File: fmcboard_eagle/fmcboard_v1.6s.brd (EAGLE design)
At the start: 147 x 74 mm, 281 parts, among them IC1 OPA699ID, IC10 LM358, IC11 7805DT, IC12 SN74AUC2G66DCTR, IC13 SN74AUC2G66DCTR, IC14 SN74AUC2G66DCTR, IC15 SN74AUC2G66DCTR, IC16 DAC7578SPWR, IC17 SN74AUC2G66DCTR, IC18 SN74AUC2G66DCTR, IC19 SN74AUC2G66DCTR, IC2 DAC7578SPWR, IC20 SN74AUC2G66DCTR, IC21 74AUP2GU04GW, IC22 74AUP2GU04GW, IC23 74AUP2GU04GW, IC24 74AUP2GU04GW, IC25 MC7905ACD2TR4G, IC26 AMS1117-1.8, IC27 LM358, IC28 SN74AUC2G66DCTR, IC29 LM337KVURG3, IC3 LTC6229IMS8E#TRPBF, IC30 SN74AUC2G66DCTR, IC31 SN74AUC2G66DCTR, IC32 SN74AUC2G66DCTR, IC33 LTC6229IMS8E#TRPBF, IC34 74AUP2GU04GW, IC35 74AUP2GU04GW, IC4 OPA695IDR, IC5 LTC6229IMS8E#TRPBF, IC6 OPA695IDR, IC7 OPA699ID, IC8 LM358, IC9 LM358, J1 8pin, J12 4p-2.54, J13 4p-2.54, J2 ASP-134604-01, J3 4p-2.54, J4 4p-2.54, J5 4p-2.54, J6 4p-2.54, J7 4p-2.54, J8 4p-2.54

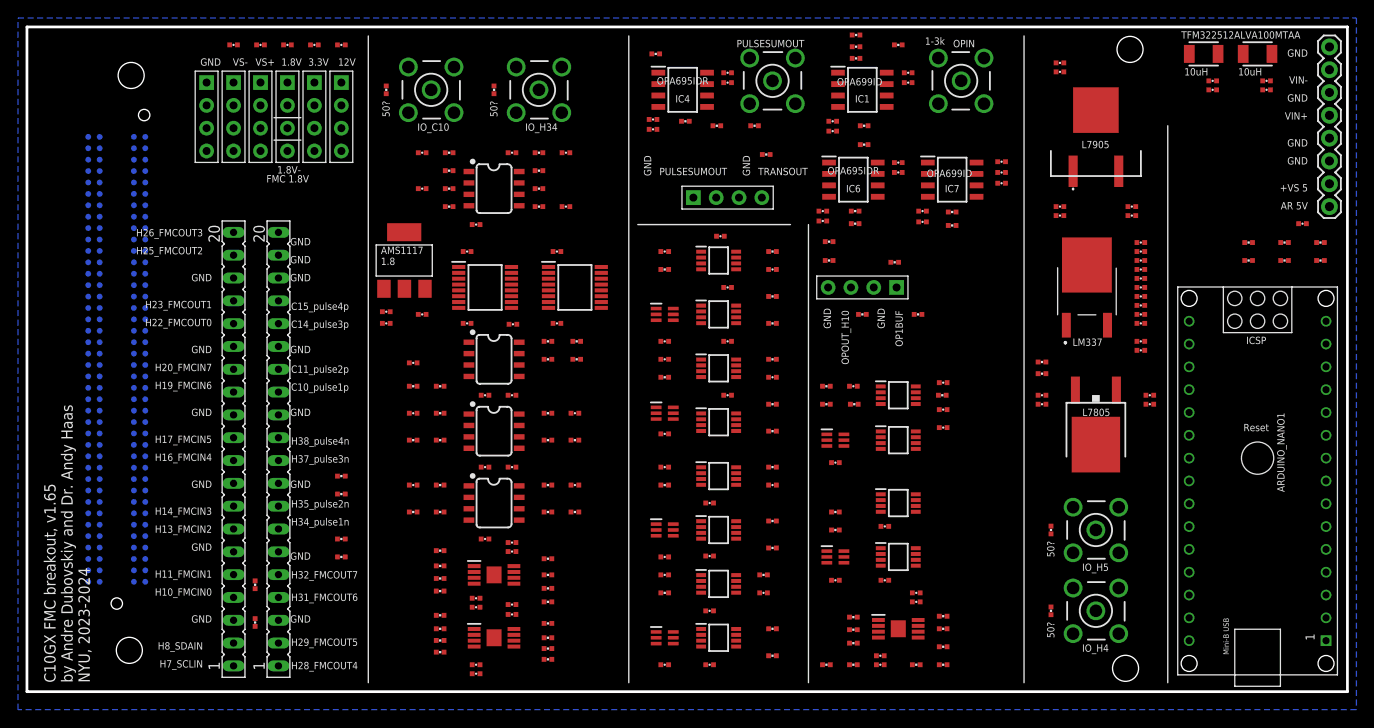
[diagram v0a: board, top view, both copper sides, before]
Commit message: and power +-7 onboard laid out
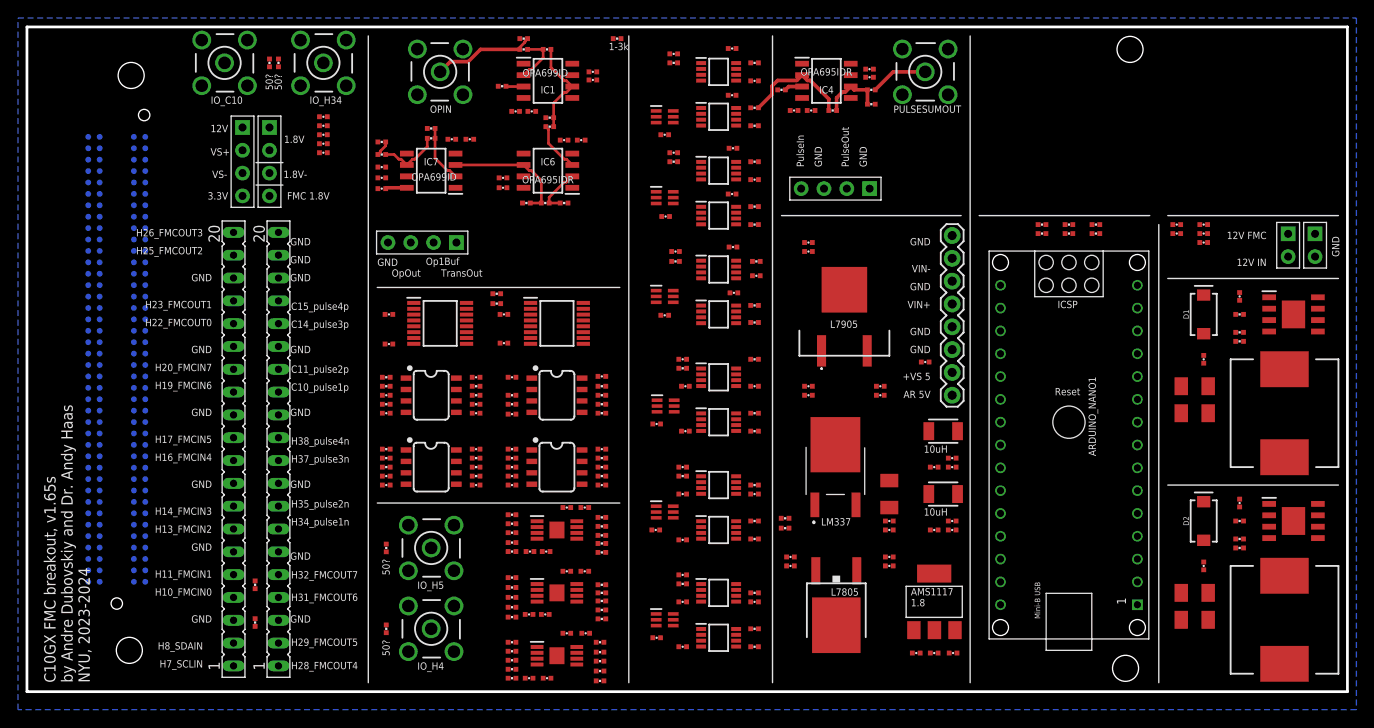
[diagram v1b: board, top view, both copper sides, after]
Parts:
- removed C110, C111, C112, C113, C114, C115: 10uF, passives:0402_CAP
- removed J4, J6, J7: 4p-2.54, Seeed-Connector:H4-2.54
- added C11, C121, C8: 0.1uF, passives:0402_CAP
- added C118, C119, C120, C64, C80: 10uF, passives:0402_CAP
- added C122: 0.01uF, passives:0402_CAP
- added C123, C124, C125: 100uF, rcl:C1206K
- added D1, D2: B340A, SparkFun-DiscreteSemi:SMA-DIODE
- added IC36, IC37: TPS5430DDAR, TPS5430DDAR:SOIC127P600X170-9N
- added J9: 2p-2.54, Seeed-Connector:H2-2.54
- added L3, L4: 10uH, SparkFun-Passives:CDRH125
- added R116, R117, R60, R84: 1k, passives:0402_RES
- added R118, R73: 10k, passives:0402_RES
- C106: value 10uF -> 0.1uF
- C107: value 10uF -> 0.01uF
- C108, C109: value 10uF -> 100uF; device passives:0402_CAP -> rcl:C1206K
- J3: value 4p-2.54 -> 2p-2.54; device Seeed-Connector:H4-2.54 -> Seeed-Connector:H2-2.54
- moved J3 112.3 mm to (143.4, 49.7)
- moved IO_H4 74.0 mm to (45.0, 7.00)
- moved IO_H5 74.0 mm to (45.0, 16.0)
- moved R15 74.0 mm to (40.0, 7.00)
- moved R16 74.0 mm to (40.0, 16.0)
- moved C74 71.2 mm to (101.0, 4.30), turned to 0 degrees
- moved C34 70.2 mm to (99.0, 4.30)
- moved IC26 70.2 mm to (101.0, 10.0)
- moved C3 70.1 mm to (103.1, 4.30), turned to 180 degrees
- moved C7 69.1 mm to (39.5, 56.0), turned to 180 degrees
- moved C28 69.0 mm to (39.5, 58.4), turned to 180 degrees
- moved C87 69.0 mm to (39.5, 57.2), turned to 180 degrees
- moved R88 62.3 mm to (39.5, 59.8)
- moved C41 60.2 mm to (103.0, 18.0)
- moved C44 60.2 mm to (103.0, 19.0)
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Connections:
- new net ARVIN: ARDUINO_NANO1.15
- new net BOOT1: C122.1, IC37.1
- new net BOOT2: C107.1, IC36.1
- new net FB1: IC37.4, R60.2, R73.1
- new net FB2: IC36.4, R116.2, R118.1
- new net N$29: C120.1, C64.2
- new net N$36: J5.2, R72.1
- new net N$39: C119.2, C41.1
- new net N$52: C120.2, C80.1
- new net N$53: C123.1, C124.2
- new net N$54: R60.1, R84.2
- new net N$55: C108.1, C109.2
- new net N$56: R116.1, R117.2
- new net SW1: C122.2, D1.C, IC37.8, L3.1
- new net SW2: C107.2, D2.C, IC36.8, L4.1
- new net V-: IC36.6, IC36.9
- net 12V: now also J9.1; no longer J8.2, J8.3, J8.4
- net 1V8-: now also C125.1; no longer C106.1, C107.1, C108.1, C109.1, C110.1, C111.1, C112.1, C113.1, C114.1, C115.1
- net 3V3: now also J8.4; no longer J3.1, J3.2, J3.3, J3.4
- net GND: now also C106.1, C109.1, C11.2, C119.1, C121.2, C123.2, C125.2, C8.2, C80.2, D1.A, IC37.6, IC37.9, J3.1, J3.2, L4.2, R118.2, R84.1; no longer C106.2, C107.2, C108.2, C109.2, C110.2, C111.2, C112.2, C113.2, C114.2, C115.2, C41.1, J4.1, J4.2, J4.3, J4.4, J5.2
- net N$38: now also C1.1, C118.2; no longer J13.4, R72.1
- net OP1BUF: now also R72.2; no longer R89.2
- net PULSESUMIN: now also J13.4
- net TRANSOUT: now also R89.2; no longer R72.2
- net VIN: now also C11.1, C64.1, C8.1, IC36.7, IC37.7, J9.2; no longer ARDUINO_NANO1.15
- net VIN+: now also C118.1, C121.1, C124.1, L3.2, R73.2; no longer C1.1
- net VIN-: now also C106.2, C108.2, D2.A, R117.1
- net VS+: now also J8.2; no longer J6.1, J6.2, J6.3, J6.4
- net VS-: now also J8.3; no longer J7.1, J7.2, J7.3, J7.4
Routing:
- net OP1BUF: track 0.00 -> 14.0 mm
- net PULSESUMIN: track 0.00 -> 12.3 mm
- net IO1: track 0.00 -> 11.5 mm
- net TRANSOUT: track 0.00 -> 10.7 mm
- net PULSESUMOUT: track 0.00 -> 7.11 mm
- net OP2OUT: track 0.00 -> 6.89 mm
- net N$11: track 0.00 -> 6.43 mm
- net PULSEOUT: track 0.00 -> 6.40 mm
- net TRANSIN: track 0.00 -> 5.65 mm
- net N$10: track 0.00 -> 5.63 mm
- net N$9: track 0.00 -> 5.41 mm
- net 1V8: track 0.00 -> 2.40 mm
- net N$8: track 0.00 -> 2.01 mm
- net N$3: track 0.00 -> 1.97 mm
- net OPOUT_H10: track 0.00 -> 1.76 mm
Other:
- board text added: "12V FMC"
- board text added: "12V IN"
- board text added: "C10GX FMC breakout, v1.65s by Andre Dubovskiy and Dr. Andy Haas NYU, 2023-2024"
- board text added: "Op1Buf"
- board text added: "OpOut"
- board text added: "PulseIn"
- board text added: "PulseOut"
- board text added: "TransOut"
- board text removed: "C10GX FMC breakout, v1.65 by Andre Dubovskiy and Dr. Andy Haas NYU, 2023-2024"
- board text removed: "OP1BUF"
- board text removed: "OPOUT_H10"
- board text removed: "PULSESUMOUT"
- board text removed: "TRANSOUT"

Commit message: power routed
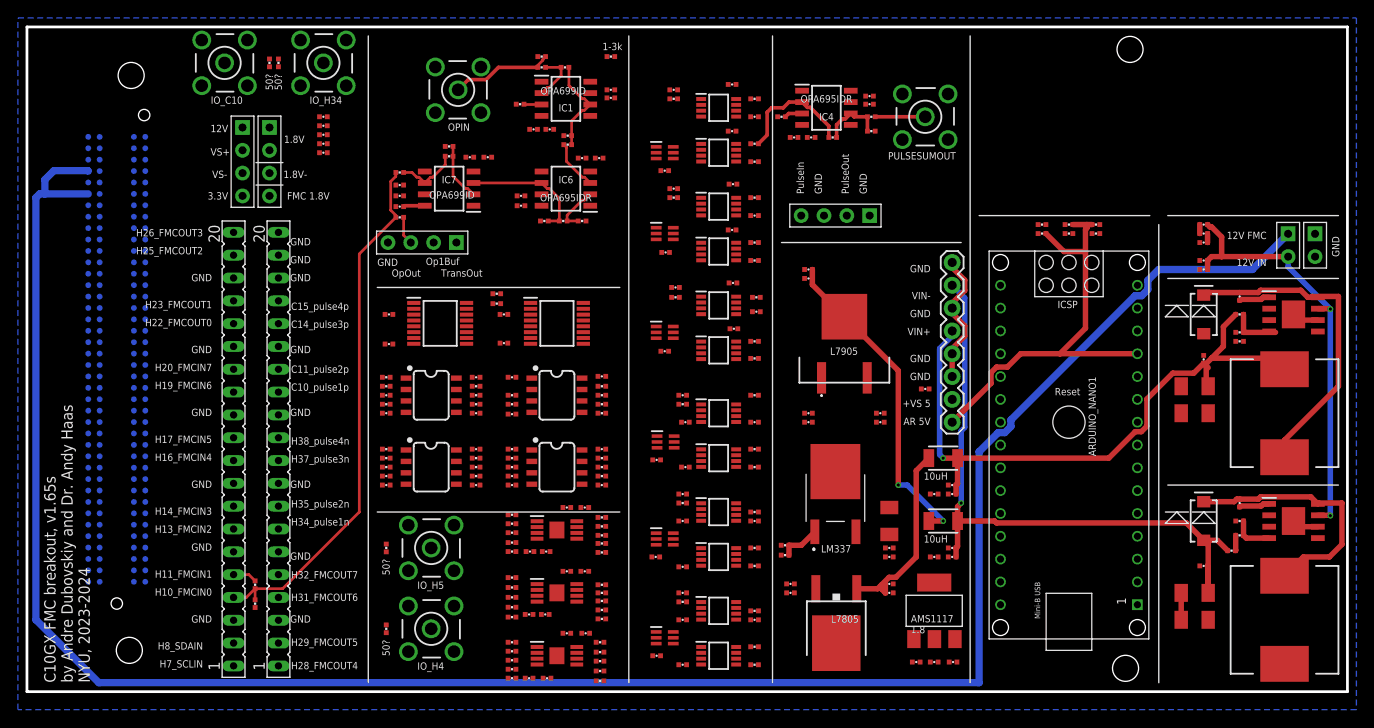
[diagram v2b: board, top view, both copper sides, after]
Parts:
- moved R86 8.63 mm to (41.5, 52.8), turned to 180 degrees
- moved C11 5.00 mm to (131.0, 48.0), turned to 180 degrees
- moved C8 5.00 mm to (131.0, 47.0), turned to 180 degrees
- moved PULSESUMOUT 5.00 mm to (100.0, 64.0)
- moved C52 4.00 mm to (78.5, 62.4)
- moved C100 4.00 mm to (81.0, 30.0)
- moved C101 4.00 mm to (73.3, 30.0)
- moved C102 4.00 mm to (78.6, 45.5)
- moved C103 4.00 mm to (78.7, 40.4)
- moved C104 4.00 mm to (73.3, 25.0)
- moved C105 4.00 mm to (71.0, 37.9)
- moved C30 4.00 mm to (70.1, 25.8)
- moved C31 4.00 mm to (81.2, 42.3)
- moved C35 4.00 mm to (78.5, 67.6)
- moved C49 4.00 mm to (71.1, 48.9)
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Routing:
- net 12V: track 0.00 -> 238.9 mm
- net VIN+: track 0.00 -> 73.4 mm, vias 0 -> 1
- net VIN-: track 0.00 -> 71.7 mm, vias 0 -> 1
- net OPOUT_H10: track 1.76 -> 59.1 mm
- net VIN: track 0.00 -> 48.1 mm, vias 0 -> 2
- net AR_5V: track 0.00 -> 47.5 mm
- net SW1: track 0.00 -> 36.7 mm
- net VIN-CLEAN: track 0.00 -> 36.2 mm, vias 0 -> 2
- net SW2: track 0.00 -> 28.4 mm
- net VIN+CLEAN: track 0.00 -> 21.7 mm
- net GND: track 0.00 -> 18.0 mm
- net FB1: track 0.00 -> 5.57 mm
- net N$30: track 0.00 -> 4.60 mm
- net FB2: track 0.00 -> 4.58 mm
- net BOOT2: track 0.00 -> 3.43 mm
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
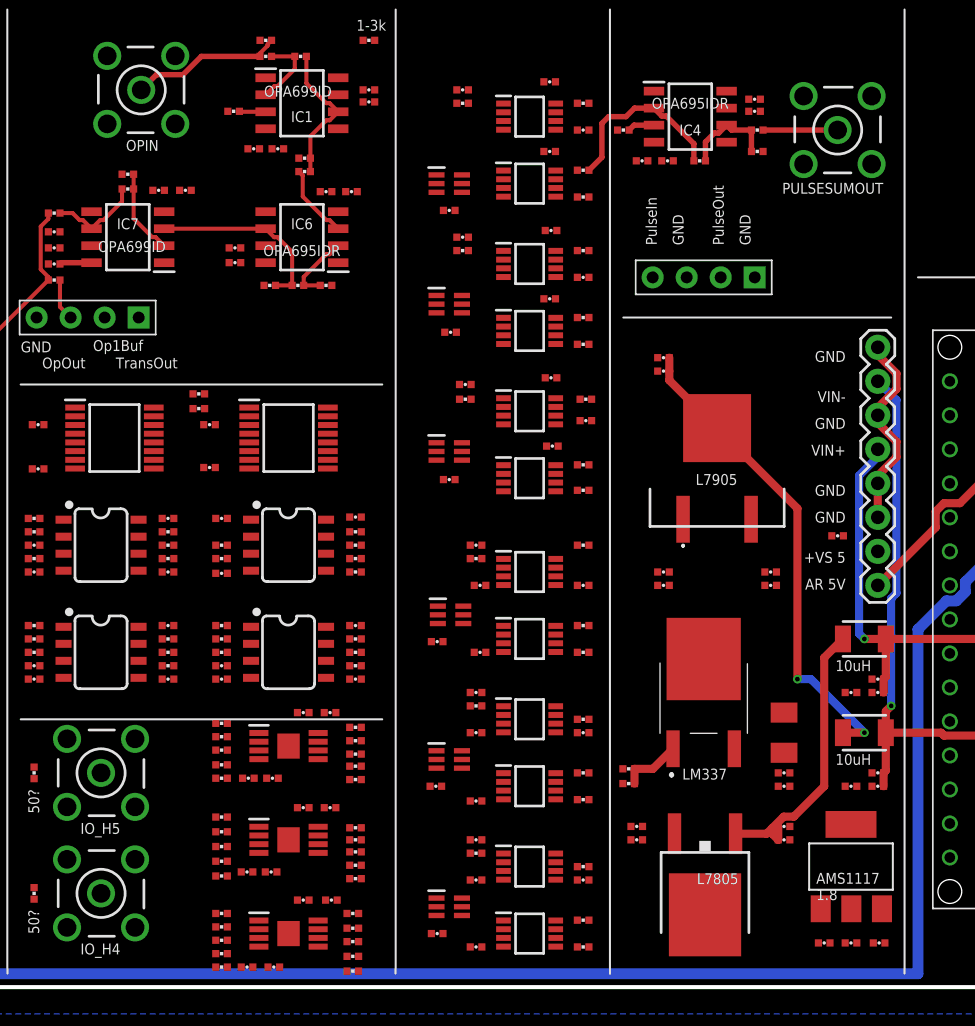
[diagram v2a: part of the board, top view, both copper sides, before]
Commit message: power routed
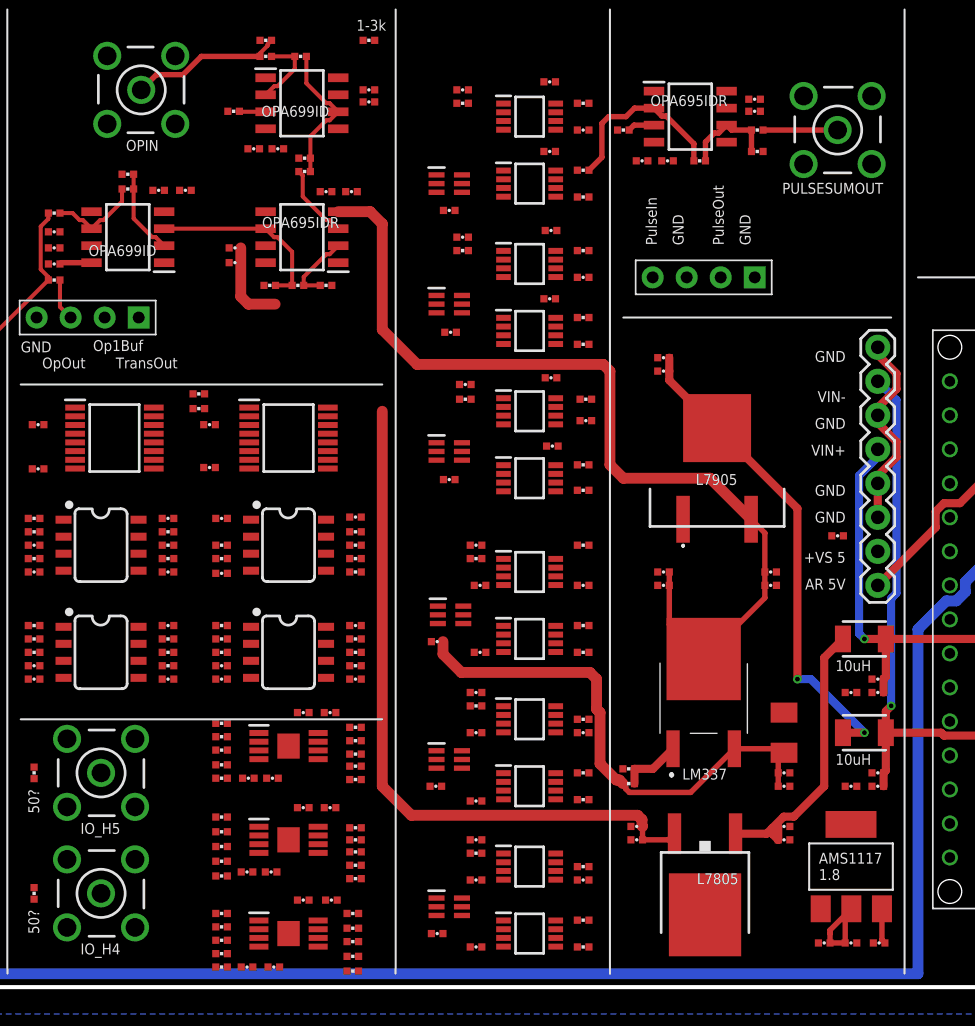
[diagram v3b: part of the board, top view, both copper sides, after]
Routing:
- net VS-: track 0.00 -> 69.4 mm
- net VS+: track 0.00 -> 61.6 mm
- net 1V8-: track 0.00 -> 38.5 mm
- net 1V8: track 2.40 -> 9.48 mm

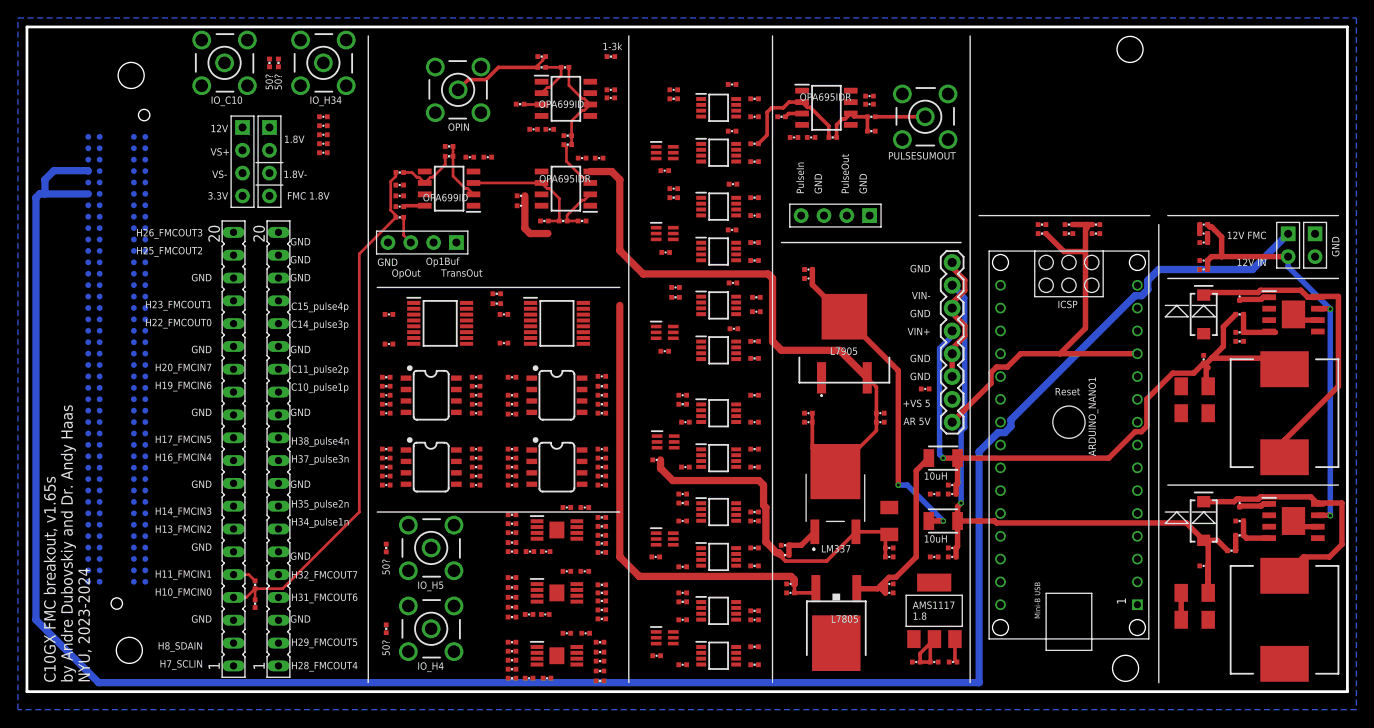
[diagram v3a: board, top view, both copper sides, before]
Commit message: power and gnd routed (with vias)
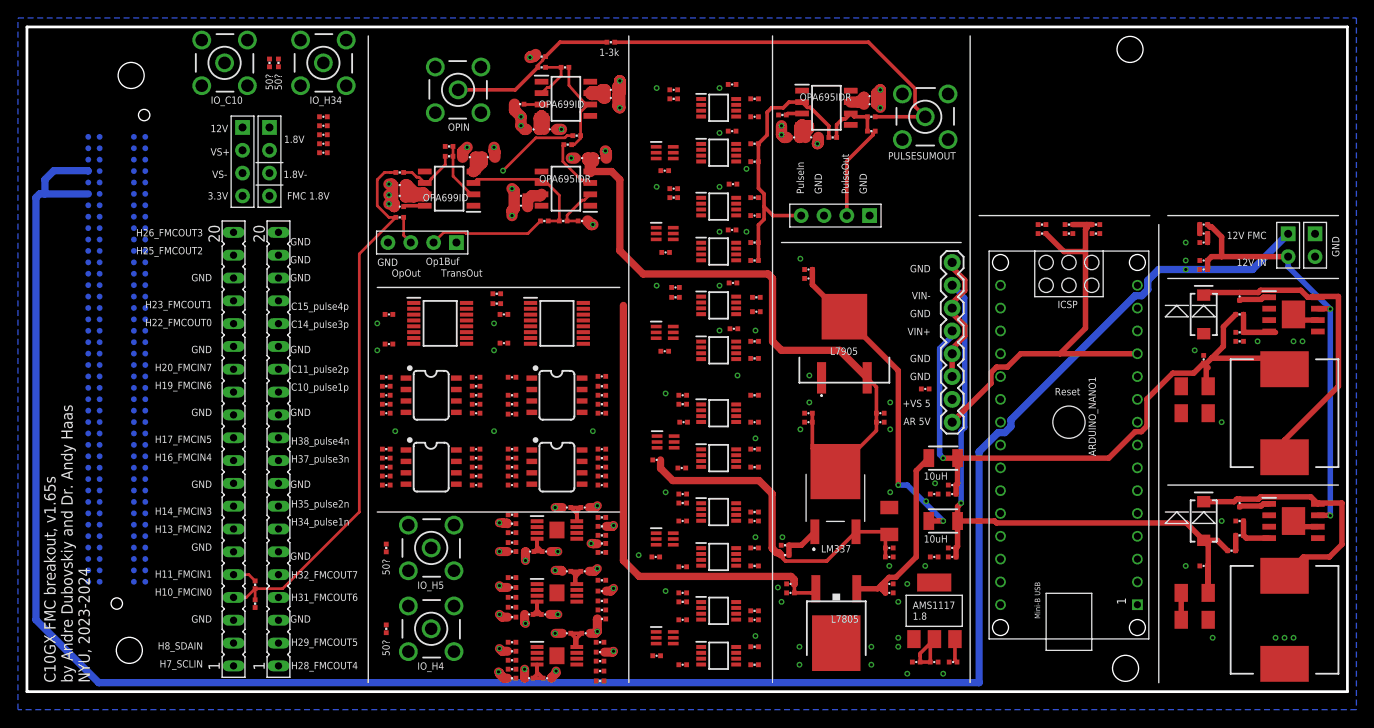
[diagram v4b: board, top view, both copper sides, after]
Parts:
- moved R9 1.60 mm to (65.0, 72.3), turned to 0 degrees
- moved R89 1.00 mm to (61.2, 61.9)
- moved R29 0.50 mm to (64.0, 12.4)
- moved C104 0.41 mm to (72.9, 24.9), turned to 180 degrees
- moved R13 0.22 mm to (84.1, 64.2)
- moved C101 0.20 mm to (73.1, 30.0), turned to 180 degrees
- moved R30 0.20 mm to (64.0, 11.2)
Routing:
- net GND: track 18.0 -> 71.2 mm, vias 0 -> 108
- net PULSEOUT: track 5.57 -> 44.7 mm
- net VS+: track 61.6 -> 85.6 mm
- net N$42: track 0.00 -> 19.5 mm, vias 0 -> 1
- net PULSESUMIN: track 13.6 -> 31.7 mm
- net VS-: track 69.4 -> 86.5 mm
- net 1V8-: track 38.5 -> 52.1 mm
- net N$36: track 0.00 -> 13.0 mm
- net N$35: track 0.00 -> 10.7 mm
- net IO1: track 11.5 -> 19.0 mm
- net OPOUT_H10: track 59.1 -> 61.6 mm
- net N$10: track 5.63 -> 6.68 mm
- net OP1BUF: track 14.0 -> 14.5 mm

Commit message: routed
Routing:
- net GND: track 71.2 -> 510.0 mm, vias 108 -> 136
- net VS+: track 85.6 -> 379.2 mm, vias 0 -> 14
- net 1V8-: track 52.1 -> 268.1 mm, vias 0 -> 11
- net 1V8: track 9.48 -> 216.0 mm, vias 0 -> 20
- net C26: track 0.00 -> 183.5 mm, vias 0 -> 2
- net C27: track 0.00 -> 173.3 mm, vias 0 -> 2
- net SCLIN: track 0.00 -> 156.9 mm, vias 0 -> 3
- net VS-: track 86.5 -> 240.4 mm, vias 0 -> 12
- net SDAIN: track 0.00 -> 153.7 mm, vias 0 -> 2
- net C10: track 0.00 -> 153.4 mm, vias 0 -> 2
- net AR_SCLIN2: track 0.00 -> 142.2 mm, vias 0 -> 6
- net AR_SDAIN2: track 0.00 -> 134.5 mm, vias 0 -> 5
- net C14: track 0.00 -> 127.8 mm, vias 0 -> 7
- net H38: track 0.00 -> 121.7 mm, vias 0 -> 3
- net N$46: track 0.00 -> 116.4 mm, vias 0 -> 4
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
